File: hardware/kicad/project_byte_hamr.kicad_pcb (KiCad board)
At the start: 4 copper layers, 144.5 x 67.3 mm, 2 parts, among them J3 Bus_Apple_II_Card_Side

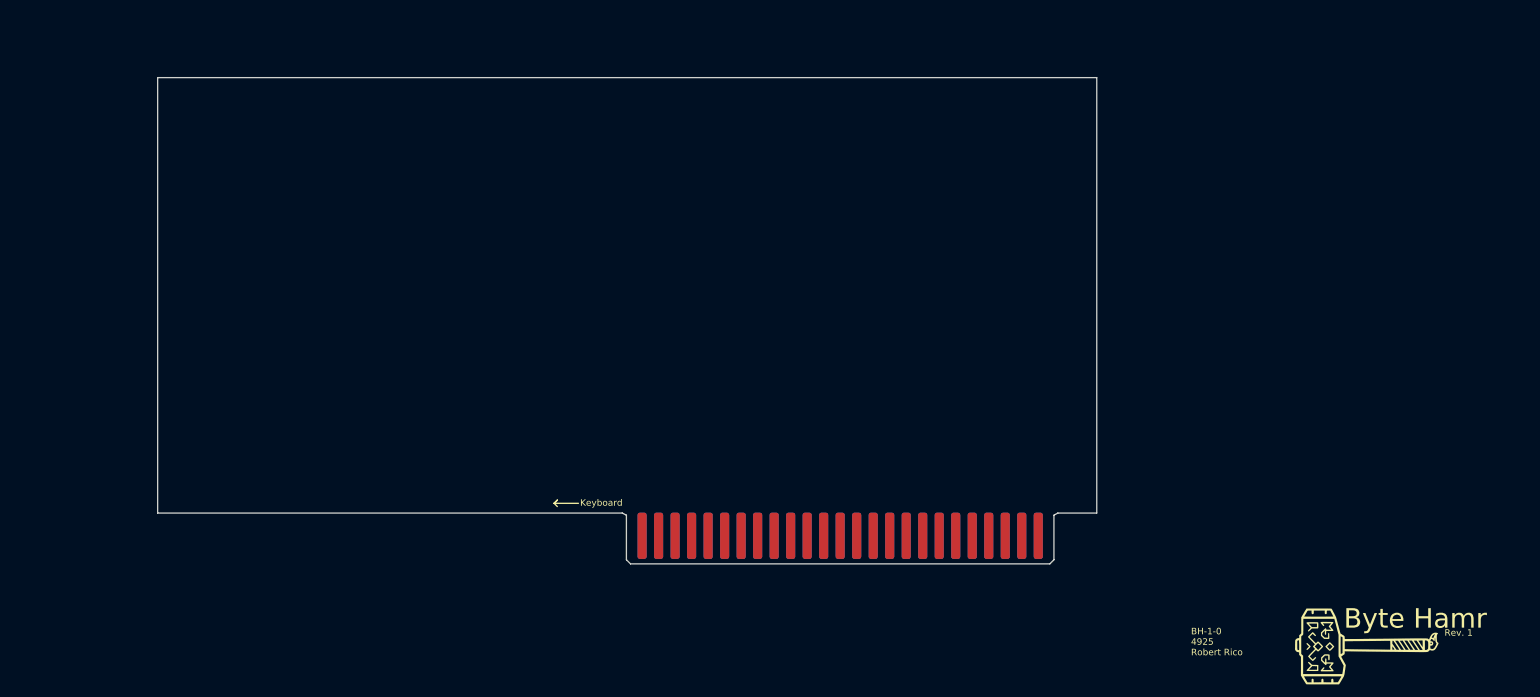
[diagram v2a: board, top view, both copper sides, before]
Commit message: Updated Rev. 1.1
- Wired Level Shifters
- Expansion GPIOs
- Oscillator
- Flash
- USB
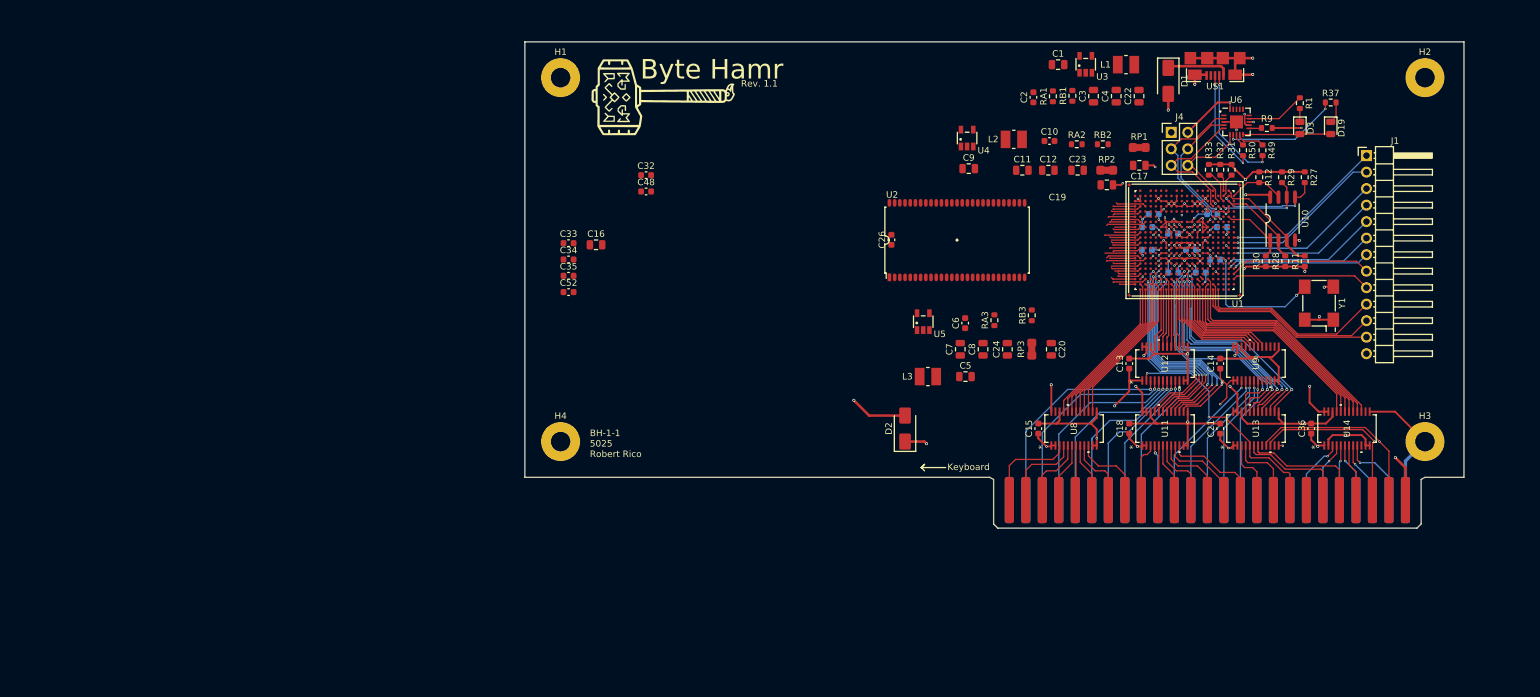
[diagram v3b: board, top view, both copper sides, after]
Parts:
- added C1: 22uF, Capacitor_SMD:C_0805_2012Metric, F.Cu at (210.6, 58.0)
- added C10: 100pF, Capacitor_SMD:C_0603_1608Metric, F.Cu at (209.2, 69.8)
- added C11: 22uF, Capacitor_SMD:C_0805_2012Metric, F.Cu at (205.1, 74.2)
- added C12: 22uF, Capacitor_SMD:C_0805_2012Metric, F.Cu at (209.1, 74.2)
- added C13: 22nF, Capacitor_SMD:C_0603_1608Metric, F.Cu at (221.5, 104.0)
- added C14: 22nF, Capacitor_SMD:C_0603_1608Metric, F.Cu at (235.5, 104.0)
- added C15: 22nF, Capacitor_SMD:C_0603_1608Metric, F.Cu at (207.5, 114.0)
- added C16: 2.2uF, Capacitor_SMD:C_0805_2012Metric, F.Cu at (139.5, 85.7)
- added C17: 2.2uF, Capacitor_SMD:C_0805_2012Metric, F.Cu at (223.1, 73.5)
- added C18: 22nF, Capacitor_SMD:C_0603_1608Metric, F.Cu at (221.5, 114.0)
- added C19: 2.2uF, Capacitor_SMD:C_0805_2012Metric, F.Cu at (218.1, 76.5)
- added C2: 100pF, Capacitor_SMD:C_0603_1608Metric, F.Cu at (206.8, 63.0)
- added C20: 2.2uF, Capacitor_SMD:C_0805_2012Metric, F.Cu at (209.5, 101.8)
- added C21: 22nF, Capacitor_SMD:C_0603_1608Metric, F.Cu at (235.5, 114.0)
- added C22: 2.2uF, Capacitor_SMD:C_0805_2012Metric, F.Cu at (223.0, 62.9)
- added C23: 2.2uF, Capacitor_SMD:C_0805_2012Metric, F.Cu at (213.6, 74.2)
- added C24: 2.2uF, Capacitor_SMD:C_0805_2012Metric, F.Cu at (202.8, 101.8)
- added C25: 22nF, Capacitor_SMD:C_0603_1608Metric, B.Cu at (224.2, 86.5)
- added C26: 22nF, Capacitor_SMD:C_0603_1608Metric, F.Cu at (184.9, 85.0)
- added C27: 22nF, Capacitor_SMD:C_0603_1608Metric, B.Cu at (231.0, 86.5)
- added C28: 22nF, Capacitor_SMD:C_0603_1608Metric, B.Cu at (228.2, 84.0)
- added C29: 22nF, Capacitor_SMD:C_0603_1608Metric, B.Cu at (234.7, 88.0)
- added C3: 22uF, Capacitor_SMD:C_0805_2012Metric, F.Cu at (216.0, 62.9)
- added C30: 22nF, Capacitor_SMD:C_0603_1608Metric, B.Cu at (225.3, 81.0)
- added C31: 22nF, Capacitor_SMD:C_0603_1608Metric, B.Cu at (228.3, 90.0)
- added C32: 22nF, Capacitor_SMD:C_0603_1608Metric, F.Cu at (147.2, 75.0)
- added C33: 22nF, Capacitor_SMD:C_0603_1608Metric, F.Cu at (135.2, 85.5)
- added C34: 22nF, Capacitor_SMD:C_0603_1608Metric, F.Cu at (135.2, 88.0)
- added C35: 22nF, Capacitor_SMD:C_0603_1608Metric, F.Cu at (135.2, 90.5)
- added C36: 22nF, Capacitor_SMD:C_0603_1608Metric, F.Cu at (249.5, 114.0)
- added C4: 22uF, Capacitor_SMD:C_0805_2012Metric, F.Cu at (219.5, 62.9)
- added C48: 22nF, Capacitor_SMD:C_0603_1608Metric, F.Cu at (147.2, 77.5)
- added C49: 22nF, Capacitor_SMD:C_0603_1608Metric, B.Cu at (224.3, 83.0)
- added C5: 22uF, Capacitor_SMD:C_0805_2012Metric, F.Cu at (196.3, 106.0)
- added C50: 22nF, Capacitor_SMD:C_0603_1608Metric, B.Cu at (235.8, 83.0)
- added C51: 22nF, Capacitor_SMD:C_0603_1608Metric, B.Cu at (234.3, 81.0)
- added C52: 22nF, Capacitor_SMD:C_0603_1608Metric, F.Cu at (135.2, 93.0)
- added C53: 22nF, Capacitor_SMD:C_0603_1608Metric, B.Cu at (232.5, 90.0)
- added C6: 100pF, Capacitor_SMD:C_0603_1608Metric, F.Cu at (196.2, 97.8)
- added C7: 22uF, Capacitor_SMD:C_0805_2012Metric, F.Cu at (195.5, 101.8)
- added C8: 22uF, Capacitor_SMD:C_0805_2012Metric, F.Cu at (199.0, 101.8)
- added C9: 22uF, Capacitor_SMD:C_0805_2012Metric, F.Cu at (196.8, 74.0)
- added D1: STPS2L40AF, Diode_SMD:D_SMA, F.Cu at (227.5, 60.5)
- added D19: RED, LED_SMD:LED_0805_2012Metric, F.Cu at (252.5, 67.8)
- added D2: STPS2L40AF, Diode_SMD:D_SMA, F.Cu at (187.0, 114.0)
- added D3: YELLOW, LED_SMD:LED_0805_2012Metric, F.Cu at (247.8, 67.8)
- added H1: MountingHole_Pad, MountingHole:MountingHole_3mm_Pad, F.Cu at (134.0, 60.0)
- added H2: MountingHole_Pad, MountingHole:MountingHole_3mm_Pad, F.Cu at (267.0, 60.0)
- added H3: MountingHole_Pad, MountingHole:MountingHole_3mm_Pad, F.Cu at (267.0, 116.0)
- added H4: MountingHole_Pad, MountingHole:MountingHole_3mm_Pad, F.Cu at (134.0, 116.0)
- added J1: Conn_01x13_Socket, Connector_PinHeader_2.54mm:PinHeader_1x13_P2.54mm_Horizontal, F.Cu at (258.0, 72.0)
- added J4: CONN_02X03, Connector_PinHeader_2.54mm:PinHeader_2x03_P2.54mm_Vertical, F.Cu at (228.0, 68.4)
- added L1: 2.2uH, L_1008_1210:L_1008_1210, F.Cu at (221.0, 58.0)
- added L2: 2.2uH, L_1008_1210:L_1008_1210, F.Cu at (203.7, 69.5)
- added L3: 2.2uH, L_1008_1210:L_1008_1210, F.Cu at (190.5, 106.0)
- added R1: 549, Resistor_SMD:R_0603_1608Metric, F.Cu at (247.8, 63.9)
- added R11: 10k, Resistor_SMD:R_0603_1608Metric, F.Cu at (248.5, 88.2)
- added R12: 10k, Resistor_SMD:R_0603_1608Metric, F.Cu at (241.5, 75.3)
- added R27: 10k, Resistor_SMD:R_0603_1608Metric, F.Cu at (248.5, 75.3)
- added R28: 10k, Resistor_SMD:R_0603_1608Metric, F.Cu at (245.5, 88.2)
- added R29: 1.1k, Resistor_SMD:R_0603_1608Metric, F.Cu at (245.0, 75.3)
- added R30: 4.7k, Resistor_SMD:R_0603_1608Metric, F.Cu at (242.5, 88.2)
- added R31: 15k, Resistor_SMD:R_0603_1608Metric, F.Cu at (237.2, 74.2)
- added R32: 15k, Resistor_SMD:R_0603_1608Metric, F.Cu at (235.5, 74.2)
- added R33: 15k, Resistor_SMD:R_0603_1608Metric, F.Cu at (233.8, 74.2)
- added R37: 549, Resistor_SMD:R_0603_1608Metric, F.Cu at (252.5, 63.8)
- added R49: 27, Resistor_SMD:R_0603_1608Metric, F.Cu at (242.0, 71.2)
- added R50: 27, Resistor_SMD:R_0603_1608Metric, F.Cu at (239.0, 71.2)
- added R9: 15k, Resistor_SMD:R_0603_1608Metric, F.Cu at (242.7, 67.8)
- added RA1: 15k, Resistor_SMD:R_0603_1608Metric, F.Cu at (209.8, 62.9)
- added RA2: 15k, Resistor_SMD:R_0603_1608Metric, F.Cu at (213.4, 70.2)
- added RA3: 15k, Resistor_SMD:R_0603_1608Metric, F.Cu at (200.8, 97.3)
- added RB1: 18k, Resistor_SMD:R_0603_1608Metric, F.Cu at (212.8, 62.8)
- added RB2: 4.7k, Resistor_SMD:R_0603_1608Metric, F.Cu at (217.4, 70.2)
- added RB3: 3.3k, Resistor_SMD:R_0603_1608Metric, F.Cu at (206.5, 96.6)
- added RP1: 0, jumper:R_0805_2012Metric_Pad1.29x1.40mm_HandSolder_Jumper_NC, F.Cu at (223.0, 70.8)
- added RP2: 0, jumper:R_0805_2012Metric_Pad1.29x1.40mm_HandSolder_Jumper_NC, F.Cu at (218.0, 74.2)
- added RP3: 0, jumper:R_0805_2012Metric_Pad1.29x1.40mm_HandSolder_Jumper_NC, F.Cu at (206.5, 101.8)
- added U1: LFE5U-25F-6BG381C, lfe5bg381:BGA-381_pitch0.8mm_dia0.4mm, F.Cu at (230.0, 85.0)
- added U10: IS25LP128F-JBLE, SOA008-150mil:SOA008-150-208mil, F.Cu at (245.1, 81.7)
- added U11: SN74LVC8T245, footprints:DBQ24-L, F.Cu at (227.0, 114.0)
- added U12: SN74LVC8T245, footprints:DBQ24-L, F.Cu at (227.0, 104.0)
- added U13: SN74LVC8T245, footprints:DBQ24-L, F.Cu at (241.0, 114.0)
- added U14: SN74LVC8T245, footprints:DBQ24-L, F.Cu at (255.0, 114.0)
- added U2: MT48LC16M16A2TG, TSOP54:TSOP54, F.Cu at (195.0, 85.0)
- added U3: TLV62569DBV, TSOT-25:TSOT-25, F.Cu at (214.8, 58.0)
- added U4: TLV62569DBV, TSOT-25:TSOT-25, F.Cu at (196.6, 69.3)
- added U5: TLV62569DBV, TSOT-25:TSOT-25, F.Cu at (189.8, 97.5)
- added U6: FT231XQ, ft231x:FT231X-QFN-20-1EP_4x4mm_P0.5mm_EP2x2mm, F.Cu at (238.0, 66.8)
- added U8: SN74LVC8T245, footprints:DBQ24-L, F.Cu at (213.0, 114.0)
- added U9: SN74LVC8T245, footprints:DBQ24-L, F.Cu at (241.0, 104.0)
- added US1: MICRO_USB, usb_otg:USB-MICRO-B-FCI-10118192-0001LF, F.Cu at (234.7, 57.0)
- added Y1: FNETHE025, oscxo:Crystal_SMD_7050_4Pads, F.Cu at (250.7, 94.7)
- moved G*** 137.3 mm to (149.8, 63.0)
- moved J3 56.8 mm to (233.5, 125.0)
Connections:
- J3 pad 22: unconnected-(J3-~{DMA}-Pad22) -> ~{DMA}_5V
- J3 pad 30: unconnected-(J3-~{IRQ}-Pad30) -> ~{IRQ}_5V
- J3 pad 39: USER1_5V -> µSync_5V
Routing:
- net GND: track 0.00 -> 231.6 mm, vias 0 -> 54
- net +3V3: track 0.00 -> 114.3 mm, vias 0 -> 27
- net CARD5V: track 0.00 -> 43.2 mm, vias 0 -> 8
- net R/~{W}_5V: track 0.00 -> 37.2 mm, vias 0 -> 2
- net +2V5: track 0.00 -> 36.8 mm, vias 0 -> 5
- net DMA_IN_3V3: track 0.00 -> 35.9 mm
- net ~{DMA}_3V3: track 0.00 -> 35.3 mm
- net ~{IRQ}_3V3: track 0.00 -> 35.1 mm
- net ~{INH}_3V3: track 0.00 -> 34.9 mm
- net A14_3V3: track 0.00 -> 34.8 mm, vias 0 -> 2
- net ~{NMI}_3V3: track 0.00 -> 34.3 mm
- net INT_IN_3V3: track 0.00 -> 34.2 mm
- net RDY_3V3: track 0.00 -> 34.1 mm, vias 0 -> 2
- net ~{RES}_3V3: track 0.00 -> 34.1 mm
- net D0_5V: track 0.00 -> 33.8 mm, vias 0 -> 1
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- added copper zone on In2.Cu, net +1V1
- added copper zone on In2.Cu, net +3V3
- added copper zone on In2.Cu, net +5V
- added copper zone on In2.Cu, net CARD5V
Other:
- board text added: "BH-1-1 5025 Robert Rico"
- board text added: "Rev. 1.1"
- board text removed: "BH-1-0 4925 Robert Rico"
- board text removed: "Rev. 1"

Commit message: Rev. 1.1
Final Revision - DRC passes
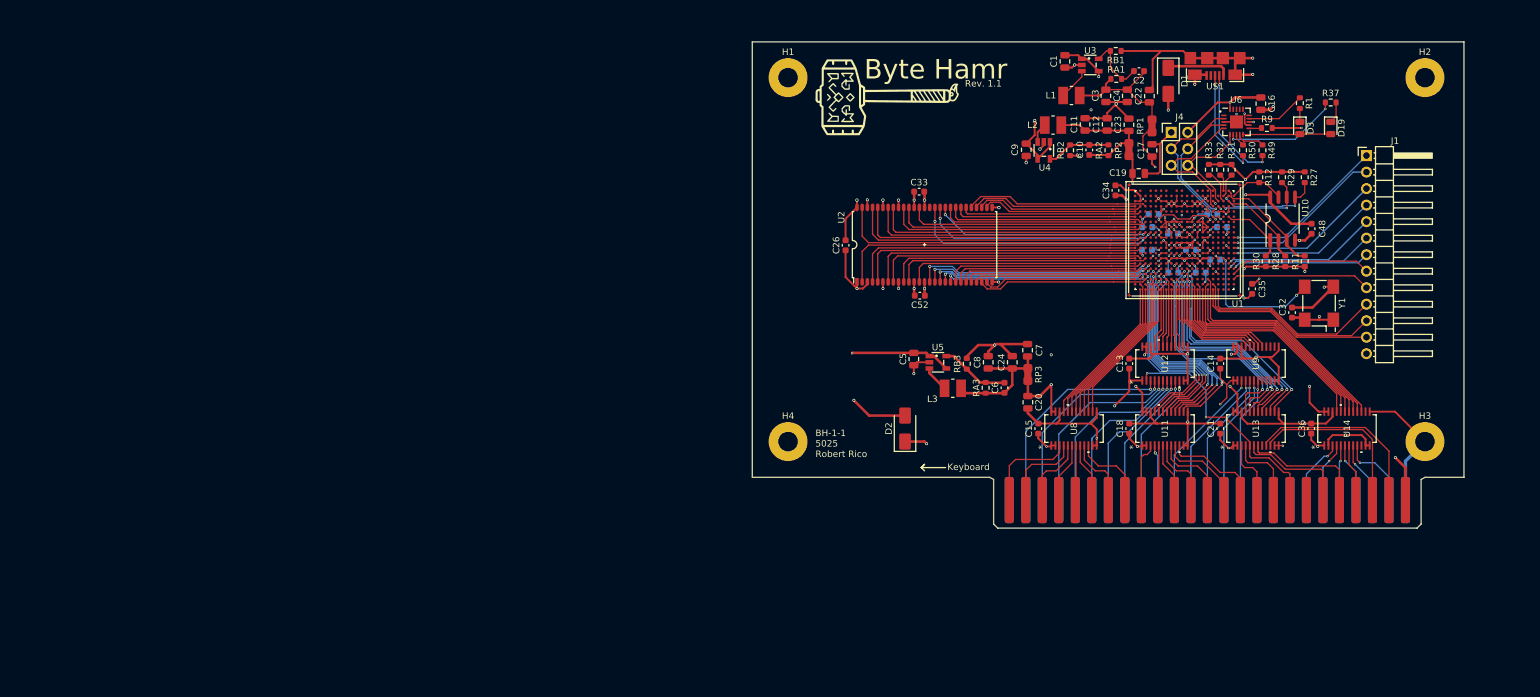
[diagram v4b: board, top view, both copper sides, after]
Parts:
- moved C35 105.2 mm to (240.4, 92.5), turned to 90 degrees
- moved C16 104.6 mm to (241.8, 64.0), turned to -90 degrees
- moved C48 102.6 mm to (249.6, 83.2), turned to -90 degrees
- moved C32 101.6 mm to (246.6, 96.2), turned to 90 degrees
- moved C34 84.8 mm to (219.4, 77.3), turned to 90 degrees
- moved C33 54.5 mm to (189.2, 77.5)
- moved C52 54.1 mm to (189.3, 93.5), turned to 180 degrees
- moved H1 35.0 mm to (169.0, 60.0)
- moved H4 35.0 mm to (169.0, 116.0)
- moved G*** 34.5 mm to (184.2, 63.0)
- moved C2 16.7 mm to (223.0, 59.0), turned to 180 degrees
- moved RB3 12.5 mm to (196.5, 104.0), turned to -90 degrees
- moved U4 12.0 mm to (208.3, 71.2), turned to 180 degrees
- moved C11 12.0 mm to (214.7, 67.2), turned to 90 degrees
- moved C6 11.6 mm to (202.3, 107.7)
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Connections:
- U1 pad C18: unconnected-(U1C-PR11A-PadC18) -> SDRAM_A2
- U1 pad C20: unconnected-(U1C-PR35A-PadC20) -> SDRAM_A3
- U1 pad D18: unconnected-(U1C-PR14A-PadD18) -> SDRAM_nCS
- U1 pad D19: unconnected-(U1C-PR35B-PadD19) -> SDRAM_A1
- U1 pad D20: unconnected-(U1C-VREF1_2-PadD20) -> SDRAM_A0
- U1 pad E17: unconnected-(U1C-PR14B-PadE17) -> SDRAM_nRAS
- U1 pad E18: unconnected-(U1C-PR14C-PadE18) -> SDRAM_nCAS
- U1 pad E19: unconnected-(U1C-PR35D-PadE19) -> SDRAM_A10
- U1 pad E20: unconnected-(U1C-PR38A-PadE20) -> SDRAM_BA1
- U1 pad F17: unconnected-(U1C-PR17A-PadF17) -> SDRAM_nWE
- U1 pad F18: unconnected-(U1C-PR14D-PadF18) -> SDRAM_DQM0
- U1 pad F19: unconnected-(U1C-PR38B-PadF19) -> SDRAM_BA0
- U1 pad F20: unconnected-(U1C-PR38C-PadF20) -> SDRAM_D7
- U1 pad G18: unconnected-(U1C-PR17B-PadG18) -> SDRAM_D6
- U1 pad G19: unconnected-(U1C-GR_PCLK2_1-PadG19) -> SDRAM_D4
- U1 pad G20: unconnected-(U1C-PR38D-PadG20) -> SDRAM_D5
- U1 pad H20: unconnected-(U1C-PR41B-PadH20) -> SDRAM_D3
- U1 pad J19: unconnected-(U1C-PCLKT2_1-PadJ19) -> SDRAM_D2
- U1 pad J20: unconnected-(U1C-PCLKT2_0-PadJ20) -> SDRAM_D1
- U1 pad K19: unconnected-(U1C-PCLKC2_1-PadK19) -> SDRAM_D0
- U1 pad K20: unconnected-(U1C-PCLKC2_0-PadK20) -> SDRAM_D15
- U1 pad L18: unconnected-(U1D-GR_PCLK3_1-PadL18) -> SDRAM_DQM1
- U1 pad L19: unconnected-(U1D-PCLKT3_0-PadL19) -> SDRAM_D14
- U1 pad L20: unconnected-(U1D-PCLKT3_1-PadL20) -> SDRAM_D13
- U1 pad M17: unconnected-(U1D-PR53B-PadM17) -> SDRAM_CLK
- U1 pad M18: unconnected-(U1D-PR50D-PadM18) -> SDRAM_CKE
- U1 pad M19: unconnected-(U1D-PCLKC3_0-PadM19) -> SDRAM_D12
- U1 pad M20: unconnected-(U1D-PCLKC3_1-PadM20) -> SDRAM_D11
- U1 pad N19: unconnected-(U1D-PR83A-PadN19) -> SDRAM_D10
- U1 pad N20: unconnected-(U1D-PR83B-PadN20) -> SDRAM_D9
- U1 pad P18: unconnected-(U1D-PR83D-PadP18) -> SDRAM_D8
- U1 pad P19: unconnected-(U1D-PR83C-PadP19) -> SDRAM_A11
- U1 pad P20: unconnected-(U1D-PR86A-PadP20) -> SDRAM_A12
- U1 pad R20: unconnected-(U1D-PR86B-PadR20) -> SDRAM_A9
- U1 pad T19: unconnected-(U1D-PR89A-PadT19) -> SDRAM_A8
- U1 pad T20: unconnected-(U1D-PR86C-PadT20) -> SDRAM_A4
- U1 pad U18: unconnected-(U1D-PR92A-PadU18) -> SDRAM_A7
- U1 pad U19: unconnected-(U1D-PR89C-PadU19) -> SDRAM_A5
- U1 pad U20: unconnected-(U1D-PR86D-PadU20) -> SDRAM_A6
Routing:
- net +3V3: track 114.3 -> 220.5 mm, vias 27 -> 35
- net GND: track 231.6 -> 337.1 mm, vias 54 -> 70
- net SDRAM_D0: track 0.00 -> 48.0 mm
- net SDRAM_D15: track 0.00 -> 46.8 mm
- net SDRAM_D14: track 0.00 -> 45.9 mm
- net SDRAM_D2: track 0.00 -> 45.1 mm
- net SDRAM_D1: track 0.00 -> 45.1 mm
- net SDRAM_D13: track 0.00 -> 44.0 mm
- net SDRAM_D12: track 0.00 -> 42.9 mm
- net SDRAM_D3: track 0.00 -> 42.1 mm
- net SDRAM_D4: track 0.00 -> 41.8 mm
- net SDRAM_D11: track 0.00 -> 40.8 mm
- net SDRAM_D6: track 0.00 -> 39.5 mm
- net SDRAM_D10: track 0.00 -> 39.5 mm
- net +5V: track 13.6 -> 52.4 mm, vias 3 -> 7
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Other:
- board size 144.5 x 67.3 mm -> 109.5 x 67.3 mm

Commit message: Updates FPGA model in BOM and schematics
Replaces LFE5U-25F-6BG381C with LFE5U-85F-8BG381I in multiple files.
Ensures consistency across BOM, schematics, and PCB layouts for the updated FPGA model.
Adjusts related properties such as part number and connectivity attributes.

Addresses a hardware specification upgrade in branch 1.1.
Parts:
- U1: value LFE5U-25F-6BG381C -> LFE5U-85F-8BG381I
